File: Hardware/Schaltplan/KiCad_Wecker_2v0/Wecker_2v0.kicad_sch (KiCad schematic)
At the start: 48 parts, among them J1 USB_C_Receptacle_PowerOnly_6P, J2 Conn_01x02_Pin, J3 Conn_01x02_Pin, J4 Conn_01x02_Pin, M1 Mühlrad, Q1 IRLML6344, Q2 IRLML6344, Q3 IRLML6344, U1 SSD1306-I2C, U2 DFPlayer_MiniMP3, U3 ESP32DevKitCv4, U4 MCP1700T-1502E/MB, U5 MCP1700T-3302E/TO

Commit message: Firmware 20v29: Ausgangs-GPIOs E1/E2/E3 getauscht (Schaltplan-Update Hardware 2v0)
Kuckuck (E1) GPIO25->GPIO27, DC-Motor/Muehlrad (E2) GPIO26->GPIO25,
LED-Streifen/Licht (E3) GPIO27->GPIO26. In der Firmware nur die Zahlenwerte
der E1/E2/E3-Konstanten in SysConf_20v29.h geaendert - die Ansteuerlogik
(digitalWrite, ledcAttach/ledcWrite, motorStart/motorStop, runCuckooMachine,
S2-Zugschalter, /motor-Handler) nutzt ausschliesslich die symbolischen
Konstanten und ist unveraendert. Motor-PWM-Kanal wandert von GPIO26 auf GPIO25.

Dokumentation nachgezogen: CHANGELOG, CLAUDE.md, README.md, Schaltplan-Notizen
(Motor-Treiber, Motor-LED-Treiber_Bauteilnotizen, Schaltplan/README).
KiCad-Schaltplan Hardware 2v0 mit aktualisierter Pin-Belegung.

Co-Authored-By: Claude Sonnet 5 <noreply@anthropic.com>
Claude-Session: https://claude.ai/code/session_01YD1NFKu8eXrE6EPc1gn86D
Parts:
- removed C6: 22nF, symbol Device:C_Small
- added C6: 10µF, symbol Device:C_Polarized_Small
- U4: value MCP1700T-1502E/MB -> MCP1702-1502TO
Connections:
- net 1,5V: now also U4.3 (VO), C6.1; no longer U4.2 (VO)
- net 5,0V: now also U4.2 (VI); no longer U4.3 (VI)
- net GNDD: now also C6.2
- net at R1.1, R4.1: now also U3.30 (27); no longer U3.28 (25)
- net at R3.1, R6.1: now also U3.28 (25); no longer U3.29 (26)
- net at R2.1, R5.1: now also U3.29 (26); no longer U3.30 (27)
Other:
- note added: "ALT: NEU: 27 LED 27 Cockoo 26 Motor 26 LED 25 Cuckoo 25 Motor"
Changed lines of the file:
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@@
 		)
 	)
+	(text "ALT:         NEU:\n27 LED       27 Cockoo\n26 Motor     26 LED\n25 Cuckoo    25 Motor"
+		(exclude_from_sim no)
+		(at 158.75 77.724 0)
+		(effects
+			(font
+				(size 1 1)
+			)
+			(justify left)
+		)
+	)
 	(text "Motor Modul"
 		(exclude_from_sim no)
@@
 		)
 	)
+	(text "Tantal"
+		(exclude_from_sim no)
+		(at 230.124 32.004 0)
+		(effects
+			(font
+				(size 1.27 1.27)
+			)
+		)
+	)
 	(text "Zugschalter"
 		(exclude_from_sim no)
@@
 	)
 	(junction
+		(at 205.74 82.55)
+		(diameter 0)
+		(color 0 0 0 0)
+	)
+	(junction
 		(at 198.12 161.29)
 		(diameter 0)
@@
 	)
 	(junction
-		(at 205.74 87.63)
+		(at 198.12 105.41)
 		(diameter 0)
 		(color 0 0 0 0)
@@
 	)
 	(junction
-		(at 198.12 105.41)
-		(diameter 0)
-		(color 0 0 0 0)
-	)
-	(junction
 		(at 200.66 50.8)
 		(diameter 0)
@@
 	(wire
 		(pts
-			(xy 213.36 50.8) (xy 213.36 54.61)
-		)
-		(stroke
-			(width 0)
-			(type default)
-		)
-	)
-	(wire
-		(pts
 			(xy 95.25 72.39) (xy 107.95 72.39)
 		)
@@
 	(wire
 		(pts
+			(xy 140.97 87.63) (xy 190.5 87.63)
+		)
+		(stroke
+			(width 0)
+			(type default)
+		)
+	)
+	(wire
+		(pts
 			(xy 200.66 25.4) (xy 205.74 25.4)
 		)
@@
 	(wire
 		(pts
-			(xy 140.97 85.09) (xy 190.5 85.09)
-		)
-		(stroke
-			(width 0)
-			(type default)
-		)
-	)
-	(wire
-		(pts
 			(xy 198.12 111.76) (xy 198.12 161.29)
 		)
@@
 	(wire
 		(pts
-			(xy 205.74 87.63) (xy 205.74 74.93)
-		)
-		(stroke
-			(width 0)
-			(type default)
-		)
-	)
-	(wire
-		(pts
 			(xy 105.41 69.85) (xy 107.95 69.85)
 		)
@@
 	(wire
 		(pts
-			(xy 205.74 88.9) (xy 205.74 87.63)
+			(xy 205.74 74.93) (xy 205.74 82.55)
 		)
 		(stroke
@@
 	(wire
 		(pts
-			(xy 190.5 85.09) (xy 190.5 151.13)
-		)
-		(stroke
-			(width 0)
-			(type default)
-		)
-	)
-	(wire
-		(pts
 			(xy 76.2 38.1) (xy 76.2 50.8)
 		)
@@
 	(wire
 		(pts
+			(xy 140.97 82.55) (xy 205.74 82.55)
+		)
+		(stroke
+			(width 0)
+			(type default)
+		)
+	)
+	(wire
+		(pts
 			(xy 81.28 105.41) (xy 81.28 95.25)
 		)
@@
 	(wire
 		(pts
+			(xy 198.12 85.09) (xy 198.12 105.41)
+		)
+		(stroke
+			(width 0)
+			(type default)
+		)
+	)
+	(wire
+		(pts
 			(xy 153.67 114.3) (xy 156.21 114.3)
 		)
@@
 	(wire
 		(pts
+			(xy 190.5 87.63) (xy 190.5 151.13)
+		)
+		(stroke
+			(width 0)
+			(type default)
+		)
+	)
+	(wire
+		(pts
 			(xy 205.74 93.98) (xy 205.74 161.29)
 		)
@@
 	(wire
 		(pts
-			(xy 140.97 87.63) (xy 205.74 87.63)
-		)
-		(stroke
-			(width 0)
-			(type default)
-		)
-	)
-	(wire
-		(pts
 			(xy 241.3 36.83) (xy 241.3 50.8)
 		)
@@
 	(wire
 		(pts
-			(xy 198.12 82.55) (xy 198.12 105.41)
-		)
-		(stroke
-			(width 0)
-			(type default)
-		)
-	)
-	(wire
-		(pts
 			(xy 213.36 62.23) (xy 213.36 92.71)
 		)
@@
 	(wire
 		(pts
-			(xy 213.36 92.71) (xy 213.36 124.46)
+			(xy 205.74 82.55) (xy 205.74 88.9)
 		)
 		(stroke
@@
 	(wire
 		(pts
-			(xy 140.97 82.55) (xy 198.12 82.55)
+			(xy 213.36 92.71) (xy 213.36 124.46)
 		)
 		(stroke
@@
 	(wire
 		(pts
+			(xy 140.97 85.09) (xy 198.12 85.09)
+		)
+		(stroke
+			(width 0)
+			(type default)
+		)
+	)
+	(wire
+		(pts
 			(xy 200.66 38.1) (xy 200.66 50.8)
 		)
@@
 			)
 		)
-		(property "Value" "MCP1700T-1502E/MB"
+		(property "Value" "MCP1702-1502TO"
 			(at 213.36 21.59 0)
 			(show_name no)
@@
 	)
 	(symbol
+		(lib_id "Device:C_Polarized_Small")
+		(at 224.79 35.56 0)
+		(unit 1)
+		(body_style 1)
+		(exclude_from_sim no)
+		(in_bom yes)
+		(on_board yes)
+		(in_pos_files yes)
+		(dnp no)
+		(property "Reference" "C6"
+			(at 227.33 34.29 0)
+			(show_name no)
+			(do_not_autoplace no)
+			(effects
+				(font
+					(size 1.27 1.27)
+				)
+				(justify left)
+			)
+		)
+		(property "Value" "10µF"
+			(at 227.33 36.83 0)
+			(show_name no)
+			(do_not_autoplace no)
+			(effects
+				(font
+					(size 1.27 1.27)
+				)
+				(justify left)
+			)
+		)
+		(property "Footprint" ""
+			(at 224.79 35.56 0)
+			(hide yes)
+			(show_name no)
+			(do_not_autoplace no)
+			(effects
+				(font
+					(size 1.27 1.27)
+				)
+			)
+		)
+		(property "Datasheet" ""
+			(at 224.79 35.56 0)
+			(hide yes)
+			(show_name no)
+			(do_not_autoplace no)
+			(effects
+				(font
+					(size 1.27 1.27)
+				)
+			)
+		)
+		(property "Description" ""
+			(at 224.79 35.56 0)
+			(show_name no)
+			(do_not_autoplace no)
+			(effects
+				(font
+					(size 1.27 1.27)
+				)
+			)
+		)
+		(pin "1"
+		)
+		(pin "2"
+		)
+		(instances
+			(project "Wecker_2v0"
+				(path "/ee0c87d8-bcc2-41db-b2ea-52ca553fb41a"
+					(reference "C6")
+					(unit 1)
+				)
+			)
+		)
+	)
+	(symbol
 		(lib_id "Device:C_Small")
 		(at 109.22 119.38 0)
@@
 		)
 		(property "Value" "22nF"
-			(at 203.2 36.8363 0)
+			(at 203.2 36.83 0)
 			(show_name no)
 			(do_not_autoplace no)
@@
 					(unit 1)
 				)
-			)
-		)
-	)
-	(symbol
-		(lib_id "Device:C_Small")
-		(at 224.79 35.56 0)
-		(unit 1)
-		(body_style 1)
-		(exclude_from_sim no)
-		(in_bom yes)
-		(on_board yes)
-		(in_pos_files yes)
-		(dnp no)
-		(property "Reference" "C6"
-			(at 227.33 34.29 0)
-			(show_name no)
-			(do_not_autoplace no)
-			(effects
-				(font
-					(size 1.27 1.27)
-				)
-				(justify left)
-			)
-		)
-		(property "Value" "22nF"
-			(at 227.33 36.8363 0)
-			(show_name no)
-			(do_not_autoplace no)
-			(effects
-				(font
-					(size 1.27 1.27)
-				)
-				(justify left)
-			)
-		)
-		(property "Footprint" ""
-			(at 224.79 35.56 0)
-			(hide yes)
-			(show_name no)
-			(do_not_autoplace no)
-			(effects
-				(font
-					(size 1.27 1.27)
-				)
-			)
-		)
-		(property "Datasheet" ""
-			(at 224.79 35.56 0)
-			(hide yes)
-			(show_name no)
-			(do_not_autoplace no)
-			(effects
-				(font
-					(size 1.27 1.27)
-				)
-			)
-		)
-		(property "Description" ""
-			(at 224.79 35.56 0)
-			(show_name no)
-			(do_not_autoplace no)
-			(effects
-				(font
-					(size 1.27 1.27)
-				)
-			)
-		)
-		(pin "1"
-		)
-		(pin "2"
-		)
-		(instances
-			(project "Wecker_2v0"
-				(path "/ee0c87d8-bcc2-41db-b2ea-52ca553fb41a"
-					(reference "C6")
-					(unit 1)
-				)

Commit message: KiCad 2v0: Gate-Widerstände R1/R2/R3 auf 470Ω, E1/E2/E3-Label aktualisiert
Gate-Reihenwiderstände der drei IRLML6344-MOSFETs (Q1/Q2/Q3) standen im
Schaltplan-Symbol noch auf 100Ω statt der dokumentierten 330Ω – jetzt
konsistent mit Stückliste/Schaltplan-Notizen auf 470Ω gesetzt.
Dazu Textlabel für E1/E2/E3-Funktionsbeschriftung aktualisiert sowie
Positionsfeinjustierung C9/C11.

Co-Authored-By: Claude Sonnet 5 <noreply@anthropic.com>
Claude-Session: https://claude.ai/code/session_01PFX3jg5htPhYmZCUmWU2SY
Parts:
- R1, R2, R3: value 100 -> 470
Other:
- note added: "Funktion: 27 Cuckoo ON/OFF 26 LED ON/OFF 25 Motor PWM"
- note removed: "ALT: NEU: 27 LED 27 Cockoo 26 Motor 26 LED 25 Cuckoo 25 Motor"
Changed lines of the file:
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@@
 		)
 	)
-	(text "ALT:         NEU:\n27 LED       27 Cockoo\n26 Motor     26 LED\n25 Cuckoo    25 Motor"
+	(text "Funktion:\n27 Cuckoo ON/OFF\n26 LED ON/OFF\n25 Motor PWM"
 		(exclude_from_sim no)
-		(at 158.75 77.724 0)
+		(at 188.976 76.2 0)
 		(effects
 			(font
@@
 		(dnp no)
 		(property "Reference" "C11"
-			(at 232.41 138.43 0)
+			(at 234.188 138.43 0)
 			(show_name no)
 			(do_not_autoplace no)
@@
 		)
 		(property "Value" "22nF"
-			(at 232.41 140.97 0)
+			(at 233.934 140.97 0)
 			(show_name no)
 			(do_not_autoplace no)
@@
 		(dnp no)
 		(property "Reference" "C9"
-			(at 213.36 138.43 0)
+			(at 212.598 138.43 0)
 			(show_name no)
 			(do_not_autoplace no)
@@
 		)
 		(property "Value" "10µF"
-			(at 212.09 140.97 0)
+			(at 211.836 140.97 0)
 			(show_name no)
 			(do_not_autoplace no)
@@
 			)
 		)
-		(property "Value" "100"
+		(property "Value" "470"
 			(at 229.87 72.39 90)
 			(show_name no)
@@
 			)
 		)
-		(property "Value" "100"
+		(property "Value" "470"
 			(at 229.87 148.59 90)
 			(show_name no)
@@
 			)
 		)
-		(property "Value" "100"
+		(property "Value" "470"
 			(at 228.6 102.87 90)
 			(show_name no)

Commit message: KiCad 2v0: DFPlayer-BUSY-Filter (R15/C14) und weitere Layout-Änderungen
Übernimmt den aktuellen KiCad-Bearbeitungsstand: neue Bauteile R15
(1kΩ), C6, C14 (100nF/4,7µF) sowie zugehörige PCB-Layout-Änderungen.

Co-Authored-By: Claude Sonnet 5 <noreply@anthropic.com>
Claude-Session: https://claude.ai/code/session_01PFX3jg5htPhYmZCUmWU2SY
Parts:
- removed C6: 10µF, symbol Device:C_Polarized_Small
- added C14: 100nF, symbol Device:C_Small
- added C6: 4,7µF, symbol Device:C_Small
- added R15: 1K, symbol Device:R_Small
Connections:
- net 1,5V: now also C6.1
- net GNDD: now also C14.2, C6.2
- net at U2.16 (BUSY): now also R15.1; no longer U3.24 (34)
- new net: C14.1, R15.2, U3.24 (34)

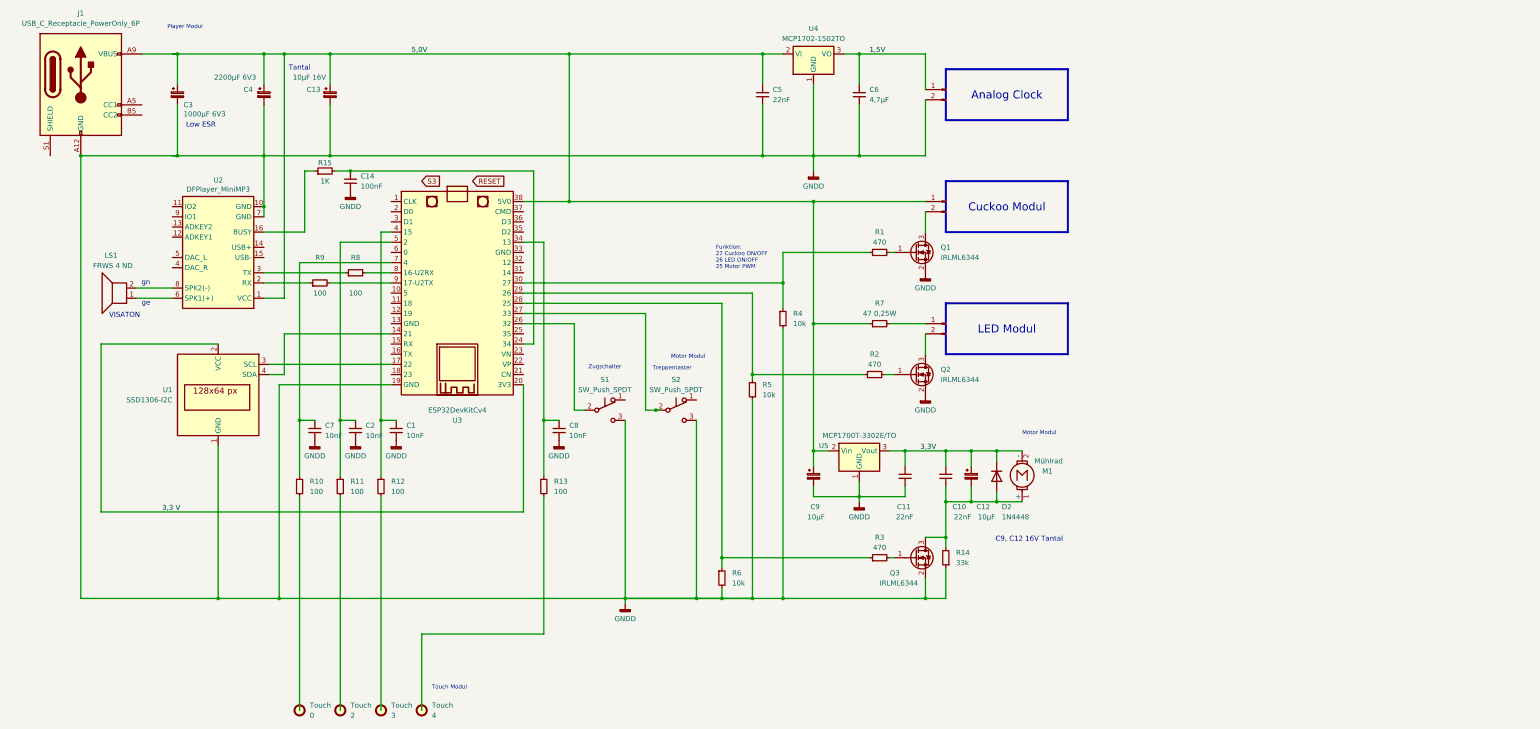
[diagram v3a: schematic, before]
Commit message: Hardware: KiCad-Layout 2v0 aktualisiert, Pin_GPIO-Liste mit PIN-Nummern, Fotos Lautsprecher-Modul, Layout.pdf
Co-Authored-By: Claude Sonnet 5.5 <noreply@anthropic.com>
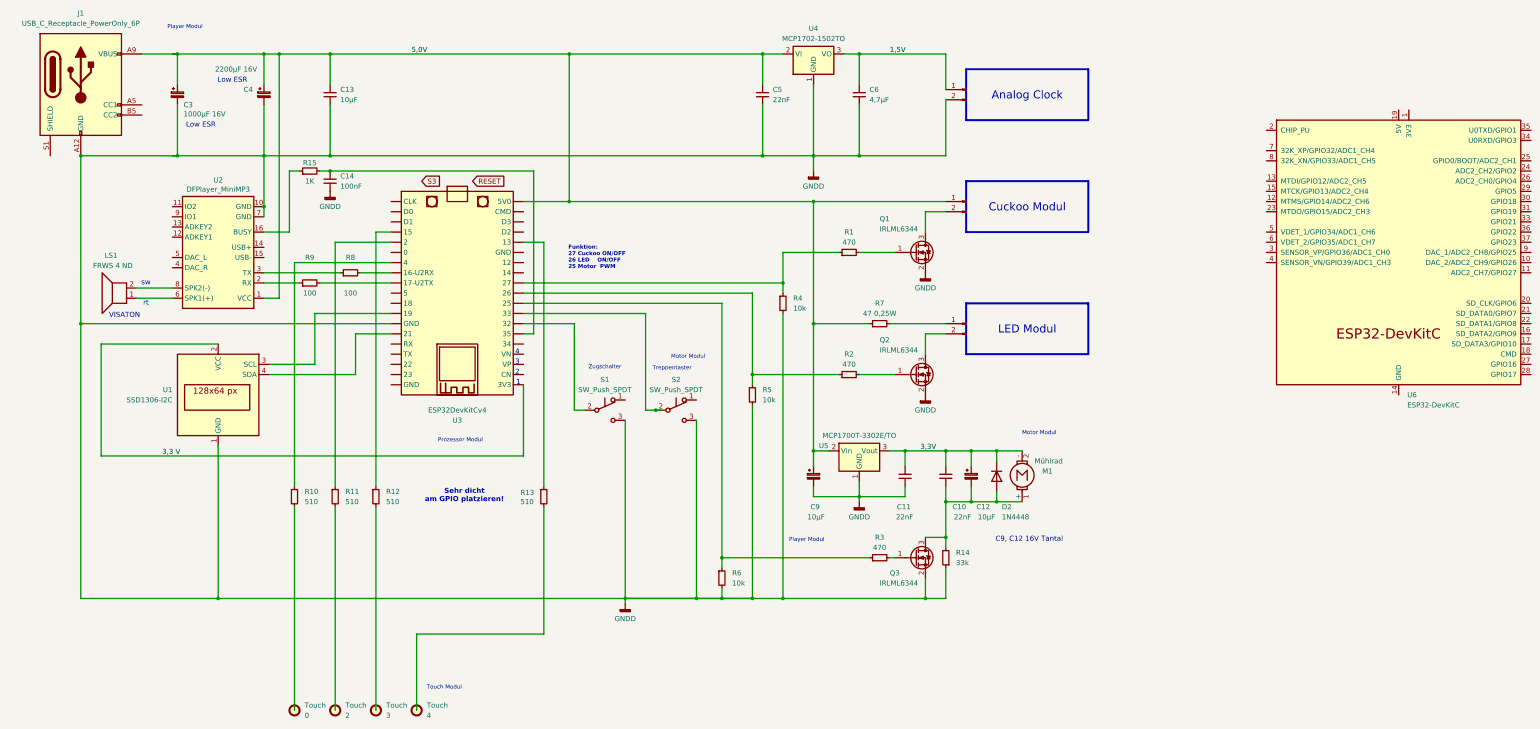
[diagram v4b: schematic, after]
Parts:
- removed C1, C2, C7, C8: 10nF, symbol Device:C_Small
- removed C13: 10µF 16V, symbol Device:C_Polarized_Small
- added C13: 10µF, symbol Device:C_Small
- added U6: ESP32-DevKitC, PCM_Espressif:ESP32-DevKitC, symbol PCM_Espressif:ESP32-DevKitC
- C3: value 1000µF 6V3 -> 1000µF 16V
- C4: value 2200µF 6V3 -> 2200µF 16V
- R10, R11, R12, R13: value 100 -> 510
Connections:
- net 5,0V: now also C13.1
- net GNDD: now also U3.13 (GND), C13.2; no longer U3.19 (GND)
- net at U3.12 (19): now also U1.3 (SCL)
- net at U3.17 (22): no longer U1.3 (SCL)
- net at C14.1, R15.2: now also U3.25 (35); no longer U3.24 (34)
- new net: U6.14 (GND), U6.32 (GND), U6.38 (GND)
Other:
- note added: "1"
- note added: "2"
- note added: "3"
- note added: "4"
- note added: "Prozessor Modul"
- note added: "Sehr dicht am GPIO platzieren!"
- note added: "rt"
- note added: "sw"
- note removed: "Tantal"
- note removed: "ge"
- note removed: "gn"
- moved on the sheet: C14, R1, R10, R11, R12, R13, R15, R2, R4, R5, R8, R9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
